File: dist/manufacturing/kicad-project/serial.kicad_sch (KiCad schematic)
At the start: 27 parts, among them J6 B8B-PH-K-S(LF)(SN), U19 TCAN332DR, U20 MAX3485EESA+T, U21 MAX3232ESE+T

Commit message: Complete orderable PD1180-EPR board release
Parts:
- removed GND (x8): GND, symbol Custom:rail_down
- removed V3V3 (x4): V3V3, symbol Custom:rail_up
- added GND (x10): GND, symbol Custom:rail_down
- added V3V3 (x5): V3V3, symbol Custom:rail_up
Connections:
- net at J6.3, J6.6: now also GND.1
- net at R75.1: now also U19.3 (VCC), V3V3.1
- net at D3.3 (K): now also C55.2, GND.1; no longer R76.2
- net at C54.2: now also GND.1; no longer D2.3
- net at U21.10 (T2IN), U21.8 (R2IN): now also GND.1
- net at C58.2, U21.15 (GND): now also GND.1
- net at U19.2 (GND): now also GND.1
- net at C54.1: now also V3V3.1; no longer U19.3 (VCC)
- net at U19.6 (CANL): now also D2.2
- net at C59.2: now also GND.1; no longer C60.2
- net at C55.1, U20.8 (VCC): now also V3V3.1
- net at U21.16 (VCC): now also V3V3.1; no longer C60.1
- net at U20.5 (GND): now also R76.2, GND.1; no longer C55.2
- net RS232_VN: no longer names the net of C59.1
- new net: C60.1, V3V3.1
- new net: C60.2, GND.1
- new net: D2.3, GND.1
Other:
- note added: "U19: 3.3 V CAN transceiver; D2: CAN TVS. U20: RS485 transceiver; D3: RS485 TVS. U21: RS232 transceiver."

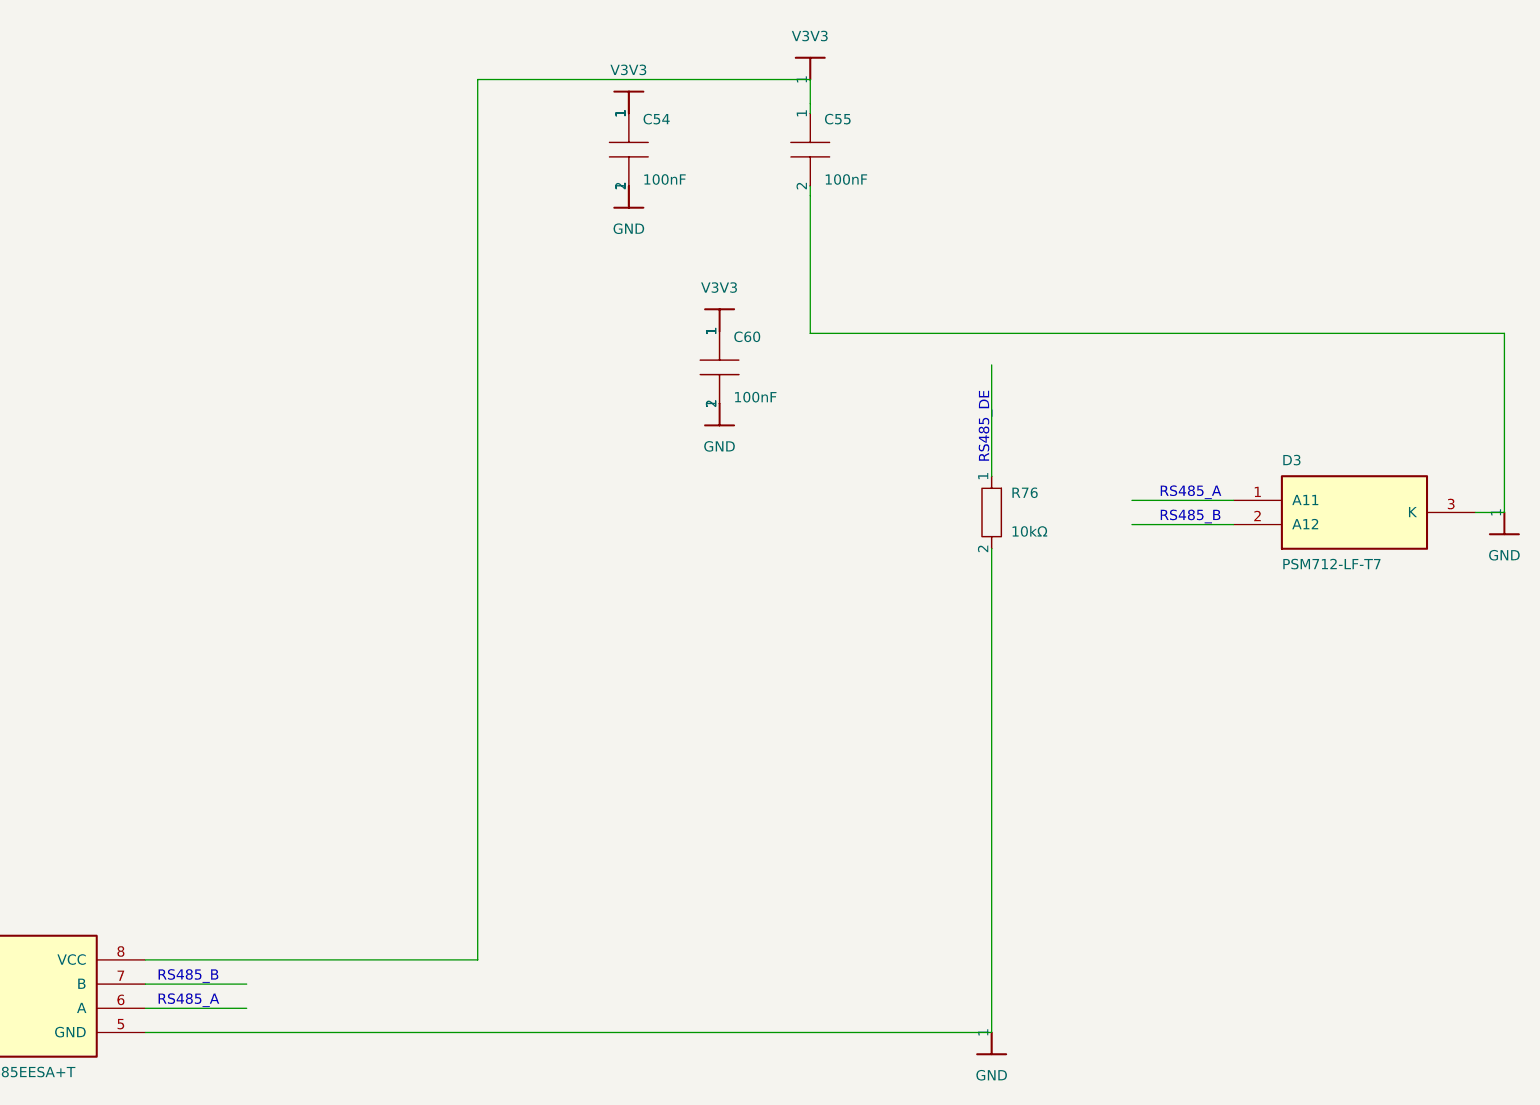
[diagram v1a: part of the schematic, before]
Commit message: Fix schematic style and top-side reset switch
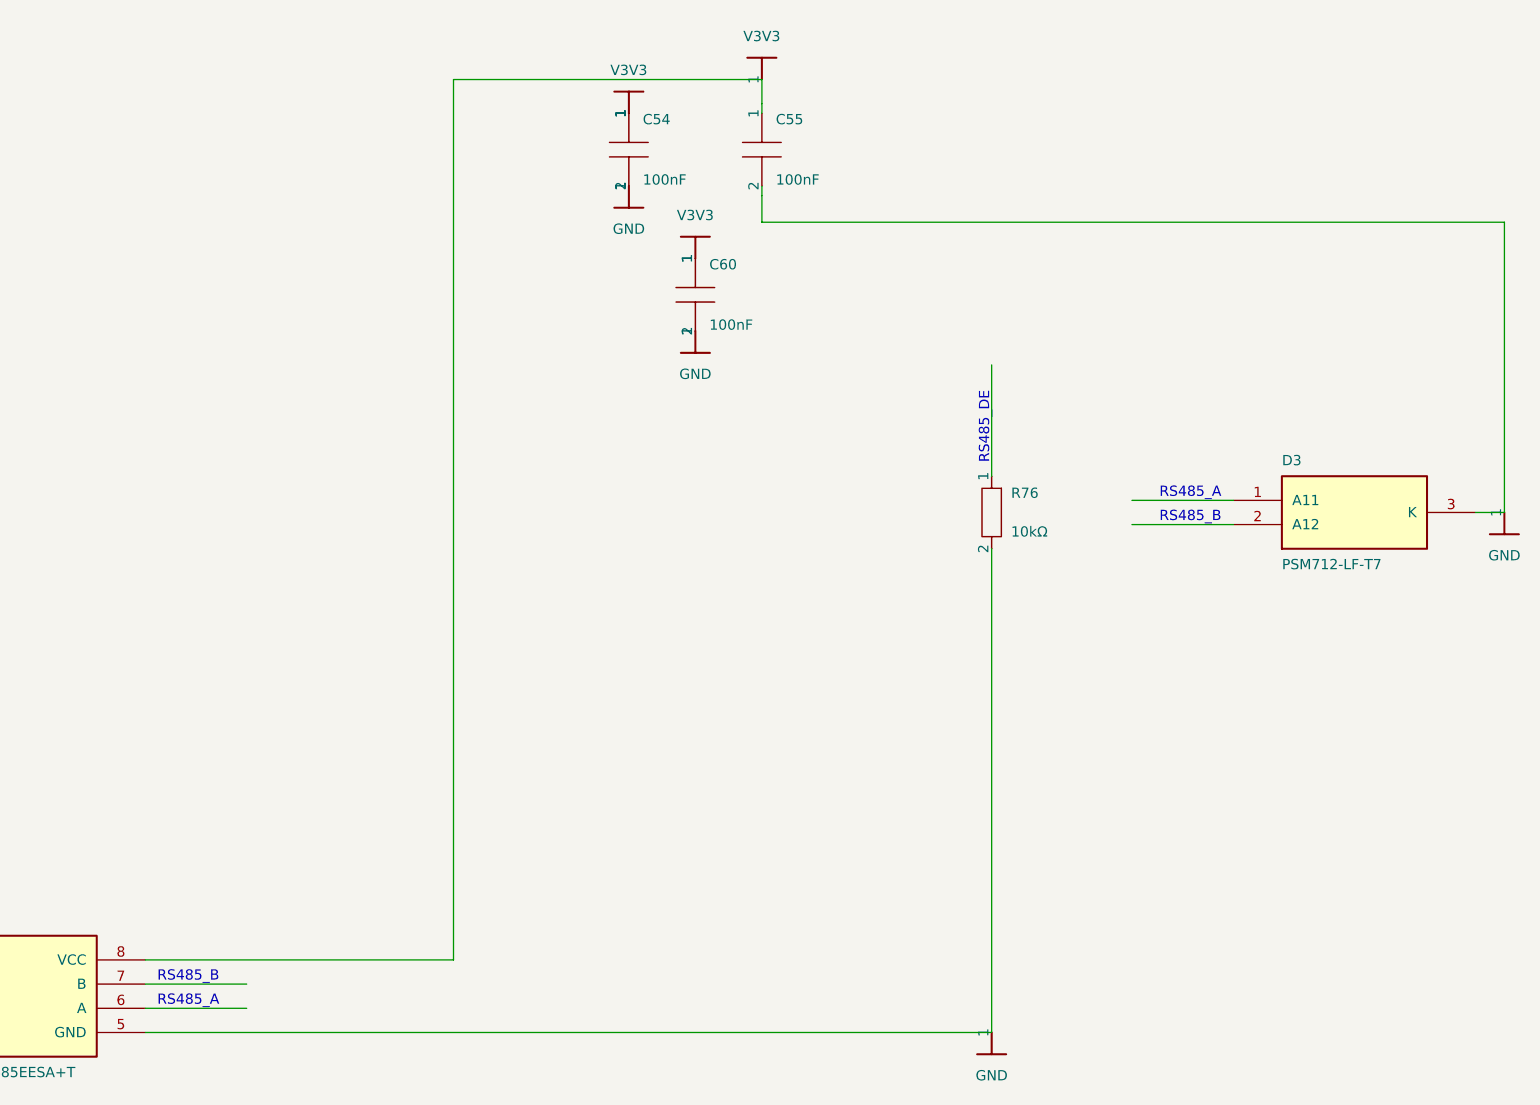
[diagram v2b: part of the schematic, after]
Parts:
- removed GND (x10): GND, symbol Custom:rail_down
- removed V3V3 (x5): V3V3, symbol Custom:rail_up
- added GND (x10): GND, symbol Custom:rail_down
- added V3V3 (x5): V3V3, symbol Custom:rail_up
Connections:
- net at C59.2: now also GND.1
- net at U19.2 (GND): now also GND.1
- net at R75.1, U19.3 (VCC): now also V3V3.1
- net at U21.10 (T2IN), U21.8 (R2IN): now also GND.1
- net at C58.2, U21.15 (GND): now also GND.1
- net at U21.16 (VCC): now also V3V3.1
- net at C60.1: now also V3V3.1
- net at C60.2: now also GND.1
- net at J6.3, J6.6: now also GND.1
- net at C54.2: now also GND.1
- net at C54.1: now also V3V3.1
- net at C55.1, U20.8 (VCC): now also V3V3.1
- net at C55.2, D3.3 (K): now also GND.1
- net at R76.2, U20.5 (GND): now also GND.1
- net at D2.3: now also GND.1

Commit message: Use one USB-C port for PD and data
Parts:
- removed GND (x10): GND, symbol Custom:rail_down
- removed V3V3 (x5): V3V3, symbol Custom:rail_up
- added GND (x10): GND, symbol Custom:rail_down
- added V3V3 (x5): V3V3, symbol Custom:rail_up
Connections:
- net at C54.2: now also GND.1
- net at U19.2 (GND): now also GND.1
- net at R75.1, U19.3 (VCC): now also V3V3.1
- net at D2.3: now also GND.1
- net at C60.1: now also V3V3.1
- net at C60.2: now also GND.1
- net at C58.2, U21.15 (GND): now also GND.1
- net at U21.10 (T2IN), U21.8 (R2IN): now also GND.1
- net at R76.2, U20.5 (GND): now also GND.1
- net at U21.16 (VCC): now also V3V3.1
- net at C54.1: now also V3V3.1
- net at C55.1, U20.8 (VCC): now also V3V3.1
- net at C59.2: now also GND.1
- net at J6.3, J6.6: now also GND.1
- net at C55.2, D3.3 (K): now also GND.1
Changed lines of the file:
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@@
     (instances
       (project ""
-        (path "/17a83a49-7a29-40ba-a4d1-006f579ceb16/36f176bd-0893-4b33-80e5-4c0c1b8c8429"
+        (path "/3270f766-a91f-4ae6-bf4b-7f3cb477ac52/97268ea4-5dde-4fbd-ae6f-8c0faae2aad8"
           (reference "U19")
           (unit 1)
@@
     (instances
       (project ""
-        (path "/17a83a49-7a29-40ba-a4d1-006f579ceb16/36f176bd-0893-4b33-80e5-4c0c1b8c8429"
+        (path "/3270f766-a91f-4ae6-bf4b-7f3cb477ac52/97268ea4-5dde-4fbd-ae6f-8c0faae2aad8"
           (reference "C54")
           (unit 1)
@@
     (instances
       (project ""
-        (path "/17a83a49-7a29-40ba-a4d1-006f579ceb16/36f176bd-0893-4b33-80e5-4c0c1b8c8429"
+        (path "/3270f766-a91f-4ae6-bf4b-7f3cb477ac52/97268ea4-5dde-4fbd-ae6f-8c0faae2aad8"
           (reference "R75")
           (unit 1)
@@
     (instances
       (project ""
-        (path "/17a83a49-7a29-40ba-a4d1-006f579ceb16/36f176bd-0893-4b33-80e5-4c0c1b8c8429"
+        (path "/3270f766-a91f-4ae6-bf4b-7f3cb477ac52/97268ea4-5dde-4fbd-ae6f-8c0faae2aad8"
           (reference "D2")
           (unit 1)
@@
     (instances
       (project ""
-        (path "/17a83a49-7a29-40ba-a4d1-006f579ceb16/36f176bd-0893-4b33-80e5-4c0c1b8c8429"
+        (path "/3270f766-a91f-4ae6-bf4b-7f3cb477ac52/97268ea4-5dde-4fbd-ae6f-8c0faae2aad8"
           (reference "U20")
           (unit 1)
@@
     (instances
       (project ""
-        (path "/17a83a49-7a29-40ba-a4d1-006f579ceb16/36f176bd-0893-4b33-80e5-4c0c1b8c8429"
+        (path "/3270f766-a91f-4ae6-bf4b-7f3cb477ac52/97268ea4-5dde-4fbd-ae6f-8c0faae2aad8"
           (reference "C55")
           (unit 1)
@@
     (instances
       (project ""
-        (path "/17a83a49-7a29-40ba-a4d1-006f579ceb16/36f176bd-0893-4b33-80e5-4c0c1b8c8429"
+        (path "/3270f766-a91f-4ae6-bf4b-7f3cb477ac52/97268ea4-5dde-4fbd-ae6f-8c0faae2aad8"
           (reference "R76")
           (unit 1)
@@
     (instances
       (project ""
-        (path "/17a83a49-7a29-40ba-a4d1-006f579ceb16/36f176bd-0893-4b33-80e5-4c0c1b8c8429"
+        (path "/3270f766-a91f-4ae6-bf4b-7f3cb477ac52/97268ea4-5dde-4fbd-ae6f-8c0faae2aad8"
           (reference "D3")
           (unit 1)
@@
     (instances
       (project ""
-        (path "/17a83a49-7a29-40ba-a4d1-006f579ceb16/36f176bd-0893-4b33-80e5-4c0c1b8c8429"
+        (path "/3270f766-a91f-4ae6-bf4b-7f3cb477ac52/97268ea4-5dde-4fbd-ae6f-8c0faae2aad8"
           (reference "U21")
           (unit 1)
@@
     (instances
       (project ""
-        (path "/17a83a49-7a29-40ba-a4d1-006f579ceb16/36f176bd-0893-4b33-80e5-4c0c1b8c8429"
+        (path "/3270f766-a91f-4ae6-bf4b-7f3cb477ac52/97268ea4-5dde-4fbd-ae6f-8c0faae2aad8"
           (reference "C56")
           (unit 1)
@@
     (instances
       (project ""
-        (path "/17a83a49-7a29-40ba-a4d1-006f579ceb16/36f176bd-0893-4b33-80e5-4c0c1b8c8429"
+        (path "/3270f766-a91f-4ae6-bf4b-7f3cb477ac52/97268ea4-5dde-4fbd-ae6f-8c0faae2aad8"
           (reference "C57")
           (unit 1)
@@
     (instances
       (project ""
-        (path "/17a83a49-7a29-40ba-a4d1-006f579ceb16/36f176bd-0893-4b33-80e5-4c0c1b8c8429"
+        (path "/3270f766-a91f-4ae6-bf4b-7f3cb477ac52/97268ea4-5dde-4fbd-ae6f-8c0faae2aad8"
           (reference "C58")
           (unit 1)
@@
     (instances
       (project ""
-        (path "/17a83a49-7a29-40ba-a4d1-006f579ceb16/36f176bd-0893-4b33-80e5-4c0c1b8c8429"
+        (path "/3270f766-a91f-4ae6-bf4b-7f3cb477ac52/97268ea4-5dde-4fbd-ae6f-8c0faae2aad8"
           (reference "C59")
           (unit 1)
@@
     (instances
       (project ""
-        (path "/17a83a49-7a29-40ba-a4d1-006f579ceb16/36f176bd-0893-4b33-80e5-4c0c1b8c8429"
+        (path "/3270f766-a91f-4ae6-bf4b-7f3cb477ac52/97268ea4-5dde-4fbd-ae6f-8c0faae2aad8"
           (reference "C60")
           (unit 1)
@@
     (instances
       (project ""
-        (path "/17a83a49-7a29-40ba-a4d1-006f579ceb16/36f176bd-0893-4b33-80e5-4c0c1b8c8429"
+        (path "/3270f766-a91f-4ae6-bf4b-7f3cb477ac52/97268ea4-5dde-4fbd-ae6f-8c0faae2aad8"
           (reference "J6")
           (unit 1)
@@
     (instances
       (project ""
-        (path "/17a83a49-7a29-40ba-a4d1-006f579ceb16/36f176bd-0893-4b33-80e5-4c0c1b8c8429"
+        (path "/3270f766-a91f-4ae6-bf4b-7f3cb477ac52/97268ea4-5dde-4fbd-ae6f-8c0faae2aad8"
           (reference "GND")
           (unit 1)
@@
     (instances
       (project ""
-        (path "/17a83a49-7a29-40ba-a4d1-006f579ceb16/36f176bd-0893-4b33-80e5-4c0c1b8c8429"
+        (path "/3270f766-a91f-4ae6-bf4b-7f3cb477ac52/97268ea4-5dde-4fbd-ae6f-8c0faae2aad8"
           (reference "GND")
           (unit 1)
@@
     (instances
       (project ""
-        (path "/17a83a49-7a29-40ba-a4d1-006f579ceb16/36f176bd-0893-4b33-80e5-4c0c1b8c8429"
+        (path "/3270f766-a91f-4ae6-bf4b-7f3cb477ac52/97268ea4-5dde-4fbd-ae6f-8c0faae2aad8"
           (reference "GND")
           (unit 1)
@@
     (instances
       (project ""
-        (path "/17a83a49-7a29-40ba-a4d1-006f579ceb16/36f176bd-0893-4b33-80e5-4c0c1b8c8429"
+        (path "/3270f766-a91f-4ae6-bf4b-7f3cb477ac52/97268ea4-5dde-4fbd-ae6f-8c0faae2aad8"
           (reference "GND")
           (unit 1)
@@
     (instances
       (project ""
-        (path "/17a83a49-7a29-40ba-a4d1-006f579ceb16/36f176bd-0893-4b33-80e5-4c0c1b8c8429"
+        (path "/3270f766-a91f-4ae6-bf4b-7f3cb477ac52/97268ea4-5dde-4fbd-ae6f-8c0faae2aad8"
           (reference "GND")
           (unit 1)
@@
     (instances
       (project ""
-        (path "/17a83a49-7a29-40ba-a4d1-006f579ceb16/36f176bd-0893-4b33-80e5-4c0c1b8c8429"
+        (path "/3270f766-a91f-4ae6-bf4b-7f3cb477ac52/97268ea4-5dde-4fbd-ae6f-8c0faae2aad8"
           (reference "GND")
           (unit 1)
@@
     (instances
       (project ""
-        (path "/17a83a49-7a29-40ba-a4d1-006f579ceb16/36f176bd-0893-4b33-80e5-4c0c1b8c8429"
+        (path "/3270f766-a91f-4ae6-bf4b-7f3cb477ac52/97268ea4-5dde-4fbd-ae6f-8c0faae2aad8"
           (reference "GND")
           (unit 1)
@@
     (instances
       (project ""
-        (path "/17a83a49-7a29-40ba-a4d1-006f579ceb16/36f176bd-0893-4b33-80e5-4c0c1b8c8429"
+        (path "/3270f766-a91f-4ae6-bf4b-7f3cb477ac52/97268ea4-5dde-4fbd-ae6f-8c0faae2aad8"
           (reference "GND")
           (unit 1)
@@
     (instances
       (project ""
-        (path "/17a83a49-7a29-40ba-a4d1-006f579ceb16/36f176bd-0893-4b33-80e5-4c0c1b8c8429"
+        (path "/3270f766-a91f-4ae6-bf4b-7f3cb477ac52/97268ea4-5dde-4fbd-ae6f-8c0faae2aad8"
           (reference "GND")
           (unit 1)
@@
     (instances
       (project ""
-        (path "/17a83a49-7a29-40ba-a4d1-006f579ceb16/36f176bd-0893-4b33-80e5-4c0c1b8c8429"
+        (path "/3270f766-a91f-4ae6-bf4b-7f3cb477ac52/97268ea4-5dde-4fbd-ae6f-8c0faae2aad8"
           (reference "GND")
           (unit 1)
@@
     (instances
       (project ""
-        (path "/17a83a49-7a29-40ba-a4d1-006f579ceb16/36f176bd-0893-4b33-80e5-4c0c1b8c8429"
+        (path "/3270f766-a91f-4ae6-bf4b-7f3cb477ac52/97268ea4-5dde-4fbd-ae6f-8c0faae2aad8"
           (reference "V3V3")
           (unit 1)
@@
     (instances
       (project ""
-        (path "/17a83a49-7a29-40ba-a4d1-006f579ceb16/36f176bd-0893-4b33-80e5-4c0c1b8c8429"
+        (path "/3270f766-a91f-4ae6-bf4b-7f3cb477ac52/97268ea4-5dde-4fbd-ae6f-8c0faae2aad8"
           (reference "V3V3")
           (unit 1)
@@
     (instances
       (project ""
-        (path "/17a83a49-7a29-40ba-a4d1-006f579ceb16/36f176bd-0893-4b33-80e5-4c0c1b8c8429"
+        (path "/3270f766-a91f-4ae6-bf4b-7f3cb477ac52/97268ea4-5dde-4fbd-ae6f-8c0faae2aad8"
           (reference "V3V3")
           (unit 1)
@@
     (instances
       (project ""
-        (path "/17a83a49-7a29-40ba-a4d1-006f579ceb16/36f176bd-0893-4b33-80e5-4c0c1b8c8429"
+        (path "/3270f766-a91f-4ae6-bf4b-7f3cb477ac52/97268ea4-5dde-4fbd-ae6f-8c0faae2aad8"
           (reference "V3V3")
           (unit 1)
@@
     (instances
       (project ""
-        (path "/17a83a49-7a29-40ba-a4d1-006f579ceb16/36f176bd-0893-4b33-80e5-4c0c1b8c8429"
+        (path "/3270f766-a91f-4ae6-bf4b-7f3cb477ac52/97268ea4-5dde-4fbd-ae6f-8c0faae2aad8"
           (reference "V3V3")
           (unit 1)

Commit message: fix: finalize single-port EPR controller
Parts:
- removed GND (x10): GND, symbol Custom:rail_down
- removed V3V3 (x5): V3V3, symbol Custom:rail_up
- C54, C55, C56, C57, C58, C59, C60: footprint (none) -> capacitor_cap0603
- D2: footprint (none) -> SM24CANB-02HTG
- D3: footprint (none) -> PSM712-LF-T7
- J6: value B8B-PH-K-S(LF)(SN) -> J6; footprint (none) -> B8B-PH-K-S_LF_SN
- R75, R76: footprint (none) -> resistor_res0603
- U19: footprint (none) -> TCAN332DR
- U20: footprint (none) -> MAX3485EESA_T
- U21: footprint (none) -> MAX3232ESE_T
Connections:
- net RS485_RX: now reaches U20.1 (RO)
- net RS485_DE: now reaches U20.2 (N_RE)
- net RS485_DE: now also R76.1, U20.3 (DE)
- net RS485_TX: now reaches U20.4 (DI)
- net GND: now reaches R76.2, U20.5 (GND)
- net GND: now also C54.2, C55.2, C58.2, C59.2, C60.2, D2.3, D3.3 (K), J6.3, J6.6, U19.2 (GND), U21.10 (T2IN), U21.15 (GND), U21.8 (R2IN)
- net RS485_A: now reaches U20.6 (A)
- net RS485_A: now also D3.1 (A11), J6.7
- net RS485_B: now reaches U20.7 (B)
- net RS485_B: now also D3.2 (A12), J6.8
- net V3V3: now reaches C55.1, U20.8 (VCC)
- net V3V3: now also C54.1, C60.1, R75.1, U19.3 (VCC), U21.16 (VCC)
- net RS232_TX_CONN: now reaches J6.1
- net RS232_TX_CONN: now also U21.14 (T1OUT)
- net RS232_RX_CONN: now reaches J6.2
- net RS232_RX_CONN: now also U21.13 (R1IN)
- net CAN_H: now reaches J6.4
- net CAN_H: now also D2.1, U19.7 (CANH)
- net CAN_L: now reaches J6.5
- net CAN_L: now also D2.2, U19.6 (CANL)
- net CAN_TX: now reaches U19.1 (TXD)
- net CAN_TX: now also R75.2
- net CAN_RX: now reaches U19.4 (RXD)
- net RS232_VN: now reaches C59.1
- net RS232_VN: now also U21.6 (V_NEG)
- net RS232_C1P: now reaches U21.1 (C1_POS)
- net RS232_C1P: now also C56.1
- net RS232_TX: now reaches U21.11 (T1IN)
- net RS232_RX: now reaches U21.12 (R1OUT)
- net RS232_VP: now reaches U21.2 (V_POS)
- net RS232_VP: now also C58.1
- net RS232_C1N: now reaches U21.3 (C1_NEG)
- net RS232_C1N: now also C56.2
- net RS232_C2P: now reaches U21.4 (C2_POS)
- net RS232_C2P: now also C57.1
- net RS232_C2N: now reaches U21.5 (C2_NEG)
- net RS232_C2N: now also C57.2
- no-connect marks 0 -> 4

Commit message: Implement dual USB power/data ECO and consolidate industrial I/O
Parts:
- removed J6: J6, B8B-PH-K-S_LF_SN, symbol Device:J_B8B-PH-K-S_LF_SN
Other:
- note added: "12 / CAN, RS485 and RS232"
- note added: "External CAN/RS485 termination; J7 carries RS232, CAN and RS485."
- note removed: "10 / CAN, RS485 and RS232"
- note removed: "External CAN/RS485 termination; J6 carries RS232, CAN and RS485."
